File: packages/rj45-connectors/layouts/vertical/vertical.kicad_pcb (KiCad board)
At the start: 2 copper layers, 1 part

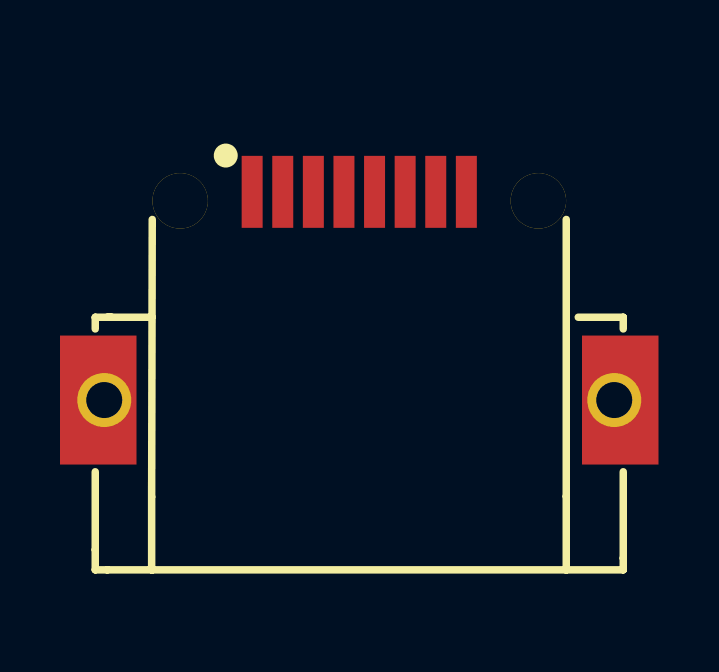
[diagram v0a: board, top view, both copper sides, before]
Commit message: fix rj45 layouts
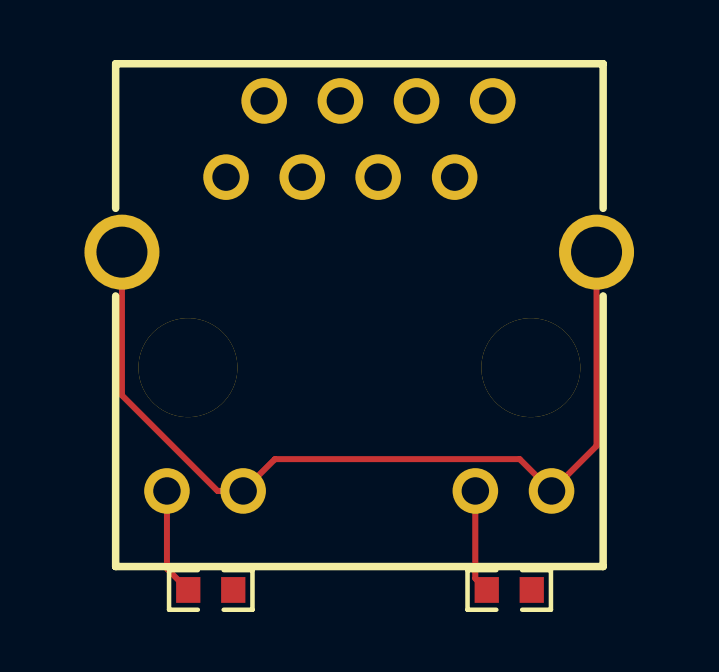
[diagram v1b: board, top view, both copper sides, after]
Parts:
- added R1: 10kΩ ±1% 100mW, UNI_ROYAL_0603WAF1002T5E:R0603, F.Cu at (151.8, 99.9)
- added R2: 10kΩ ±1% 100mW, UNI_ROYAL_0603WAF1002T5E:R0603, F.Cu at (161.7, 99.9)
- RJ1: footprint HCTL_HC_RJ45_055_7:RJ45-SMD_HC-RJ45-055-7_1 -> Ckmtw_R_RJ45S08P_C000:RJ45-TH_R-RJ45S08P-C000
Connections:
- RJ1 pad 9: GND -> Ypos
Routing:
- net GND: track 0.00 -> 29.9 mm
- net Ypos: track 0.00 -> 3.59 mm
- net Gpos: track 0.00 -> 3.46 mm

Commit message: fix rj45 connectors
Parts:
- R1, R2: value 10kΩ ±1% 100mW -> 10000.0Ω
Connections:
- net ETH_LED_LINK renamed ethernet-line-0
- net ETH_LED_SPEED renamed ethernet-line-1
- net ETH_P0_N renamed <bound method has_net_name_affix.get_prefix of <has_net_name_affix '0xF870F.ethernet.pairs[0].net_name_suffixes[1]' on <Node[Electrical] '0xF870F.ethernet.pairs[0].n.line'>>>2<bound method has_net_nam...[Electrical] '0xF870F.ethernet.pairs[0].n.line'>>>
- net ETH_P0_P renamed <bound method has_net_name_affix.get_prefix of <has_net_name_affix '0xF870F.ethernet.pairs[0].net_name_suffixes[0]' on <Node[Electrical] '0xF870F.ethernet.pairs[0].p.line'>>>1<bound method has_net_nam...[Electrical] '0xF870F.ethernet.pairs[0].p.line'>>>
- net ETH_P1_N renamed <bound method has_net_name_affix.get_prefix of <has_net_name_affix '0xF870F.ethernet.pairs[1].net_name_suffixes[1]' on <Node[Electrical] '0xF870F.ethernet.pairs[1].n.line'>>>6<bound method has_net_nam...[Electrical] '0xF870F.ethernet.pairs[1].n.line'>>>
- net ETH_P1_P renamed <bound method has_net_name_affix.get_prefix of <has_net_name_affix '0xF870F.ethernet.pairs[1].net_name_suffixes[0]' on <Node[Electrical] '0xF870F.ethernet.pairs[1].p.line'>>>3<bound method has_net_nam...[Electrical] '0xF870F.ethernet.pairs[1].p.line'>>>
- net ETH_P2_N renamed <bound method has_net_name_affix.get_prefix of <has_net_name_affix '0xF870F.ethernet.pairs[2].net_name_suffixes[1]' on <Node[Electrical] '0xF870F.ethernet.pairs[2].n.line'>>>5<bound method has_net_nam...[Electrical] '0xF870F.ethernet.pairs[2].n.line'>>>
- net ETH_P2_P renamed <bound method has_net_name_affix.get_prefix of <has_net_name_affix '0xF870F.ethernet.pairs[2].net_name_suffixes[0]' on <Node[Electrical] '0xF870F.ethernet.pairs[2].p.line'>>>4<bound method has_net_nam...[Electrical] '0xF870F.ethernet.pairs[2].p.line'>>>
- net ETH_P3_N renamed <bound method has_net_name_affix.get_prefix of <has_net_name_affix '0xF870F.ethernet.pairs[3].net_name_suffixes[1]' on <Node[Electrical] '0xF870F.ethernet.pairs[3].n.line'>>>8<bound method has_net_nam...[Electrical] '0xF870F.ethernet.pairs[3].n.line'>>>
- net ETH_P3_P renamed <bound method has_net_name_affix.get_prefix of <has_net_name_affix '0xF870F.ethernet.pairs[3].net_name_suffixes[0]' on <Node[Electrical] '0xF870F.ethernet.pairs[3].p.line'>>>7<bound method has_net_nam...[Electrical] '0xF870F.ethernet.pairs[3].p.line'>>>
- net GND renamed ethernet-lv-1

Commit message: fix conflict markers in autognerated files
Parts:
- R1, R2: value 10000.0Ω -> 10kΩ ±1% 100mW
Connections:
- net <bound method has_net_name_affix.get_prefix of <has_net_name_affix '0xF870F.ethernet.pairs[0].net_name_suffixes[0]' on <Node[Electrical] '0xF870F.ethernet.pairs[0].p.line'>>>1<bound method has_net_nam...[Electrical] '0xF870F.ethernet.pairs[0].p.line'>>> renamed ETH_P0_P
- net <bound method has_net_name_affix.get_prefix of <has_net_name_affix '0xF870F.ethernet.pairs[0].net_name_suffixes[1]' on <Node[Electrical] '0xF870F.ethernet.pairs[0].n.line'>>>2<bound method has_net_nam...[Electrical] '0xF870F.ethernet.pairs[0].n.line'>>> renamed ETH_P0_N
- net <bound method has_net_name_affix.get_prefix of <has_net_name_affix '0xF870F.ethernet.pairs[1].net_name_suffixes[0]' on <Node[Electrical] '0xF870F.ethernet.pairs[1].p.line'>>>3<bound method has_net_nam...[Electrical] '0xF870F.ethernet.pairs[1].p.line'>>> renamed ETH_P1_P
- net <bound method has_net_name_affix.get_prefix of <has_net_name_affix '0xF870F.ethernet.pairs[1].net_name_suffixes[1]' on <Node[Electrical] '0xF870F.ethernet.pairs[1].n.line'>>>6<bound method has_net_nam...[Electrical] '0xF870F.ethernet.pairs[1].n.line'>>> renamed ETH_P1_N
- net <bound method has_net_name_affix.get_prefix of <has_net_name_affix '0xF870F.ethernet.pairs[2].net_name_suffixes[0]' on <Node[Electrical] '0xF870F.ethernet.pairs[2].p.line'>>>4<bound method has_net_nam...[Electrical] '0xF870F.ethernet.pairs[2].p.line'>>> renamed ETH_P2_P
- net <bound method has_net_name_affix.get_prefix of <has_net_name_affix '0xF870F.ethernet.pairs[2].net_name_suffixes[1]' on <Node[Electrical] '0xF870F.ethernet.pairs[2].n.line'>>>5<bound method has_net_nam...[Electrical] '0xF870F.ethernet.pairs[2].n.line'>>> renamed ETH_P2_N
- net <bound method has_net_name_affix.get_prefix of <has_net_name_affix '0xF870F.ethernet.pairs[3].net_name_suffixes[0]' on <Node[Electrical] '0xF870F.ethernet.pairs[3].p.line'>>>7<bound method has_net_nam...[Electrical] '0xF870F.ethernet.pairs[3].p.line'>>> renamed ETH_P3_P
- net <bound method has_net_name_affix.get_prefix of <has_net_name_affix '0xF870F.ethernet.pairs[3].net_name_suffixes[1]' on <Node[Electrical] '0xF870F.ethernet.pairs[3].n.line'>>>8<bound method has_net_nam...[Electrical] '0xF870F.ethernet.pairs[3].n.line'>>> renamed ETH_P3_N
- net ethernet-line-0 renamed ETH_LED_LINK
- net ethernet-line-1 renamed ETH_LED_SPEED
- net ethernet-lv-1 renamed GND

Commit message: update parts
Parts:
- R1, R2: value 10kΩ ±1% 100mW -> {ℝ+}Ω
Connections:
- net ETH_P0_N renamed ETH_N0_N
- net ETH_P1_N renamed ETH_N1_N
- net ETH_P2_N renamed ETH_N2_N
- net ETH_P3_N renamed ETH_N3_N
- net GND renamed lv
